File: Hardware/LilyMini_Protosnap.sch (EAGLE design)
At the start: 67 parts, among them Q1 ZXMP6A13F, U1 SAMD11D14A-M, U2 AP2112K-3.3V, U3 ALS-PT19, Y1 32.768kHz

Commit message: Minor tweaks per board review checklist
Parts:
- added LOGO4: SFE_LOGO_NAME.1_INCH, SparkFun-Aesthetics:SFE_LOGO_NAME.1_INCH
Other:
- note added: "NOTE: DO NOT BACKPOWER BOARD THROUGH SEWTAP+ (OUTPUT ONLY) USE AUX VIN (3.5 TO 6V, AVOID CONTENTION WITH USB)"
- note removed: "NOTE: DO NOT BACKPOWER BOARD THROUGH SEWTAP+ (OUTPUT ONLY) USE AUX VIN (3.5 TO 6V)"
- moved on the sheet: D3, D4, D5, D6, R10, R6, R7, R8, R9, S2, U3

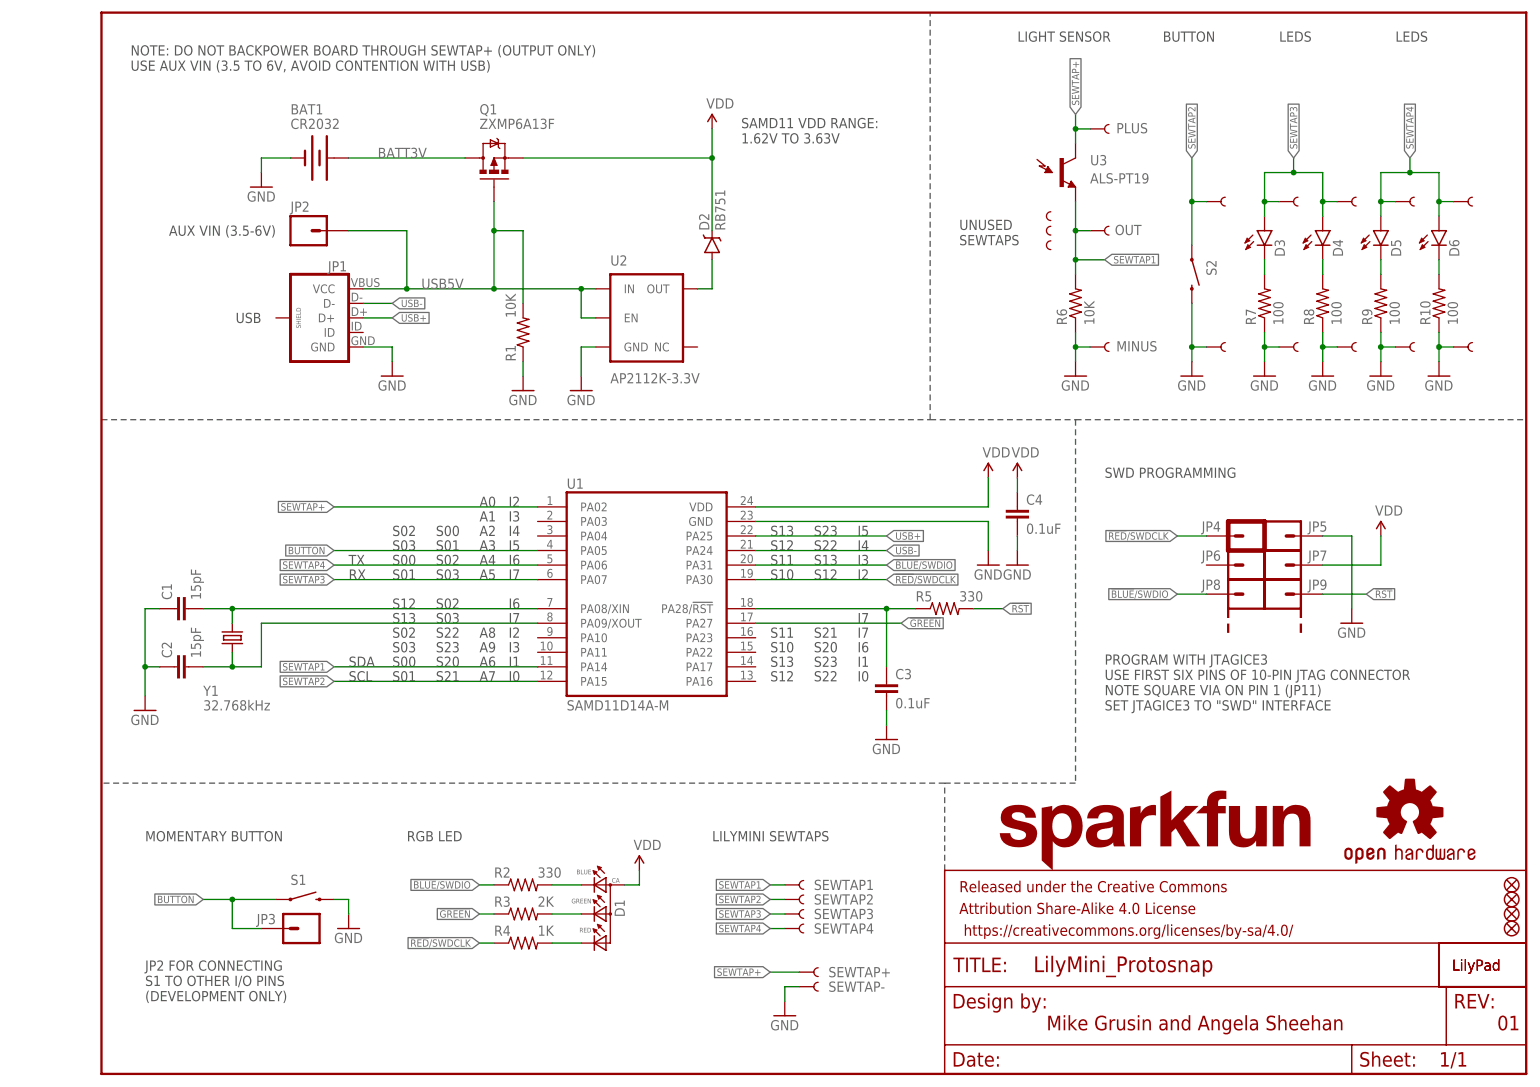
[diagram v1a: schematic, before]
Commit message: Minor changes based on AC and Bob's advice
Reduced paste on QFN and USB footprints by 25%
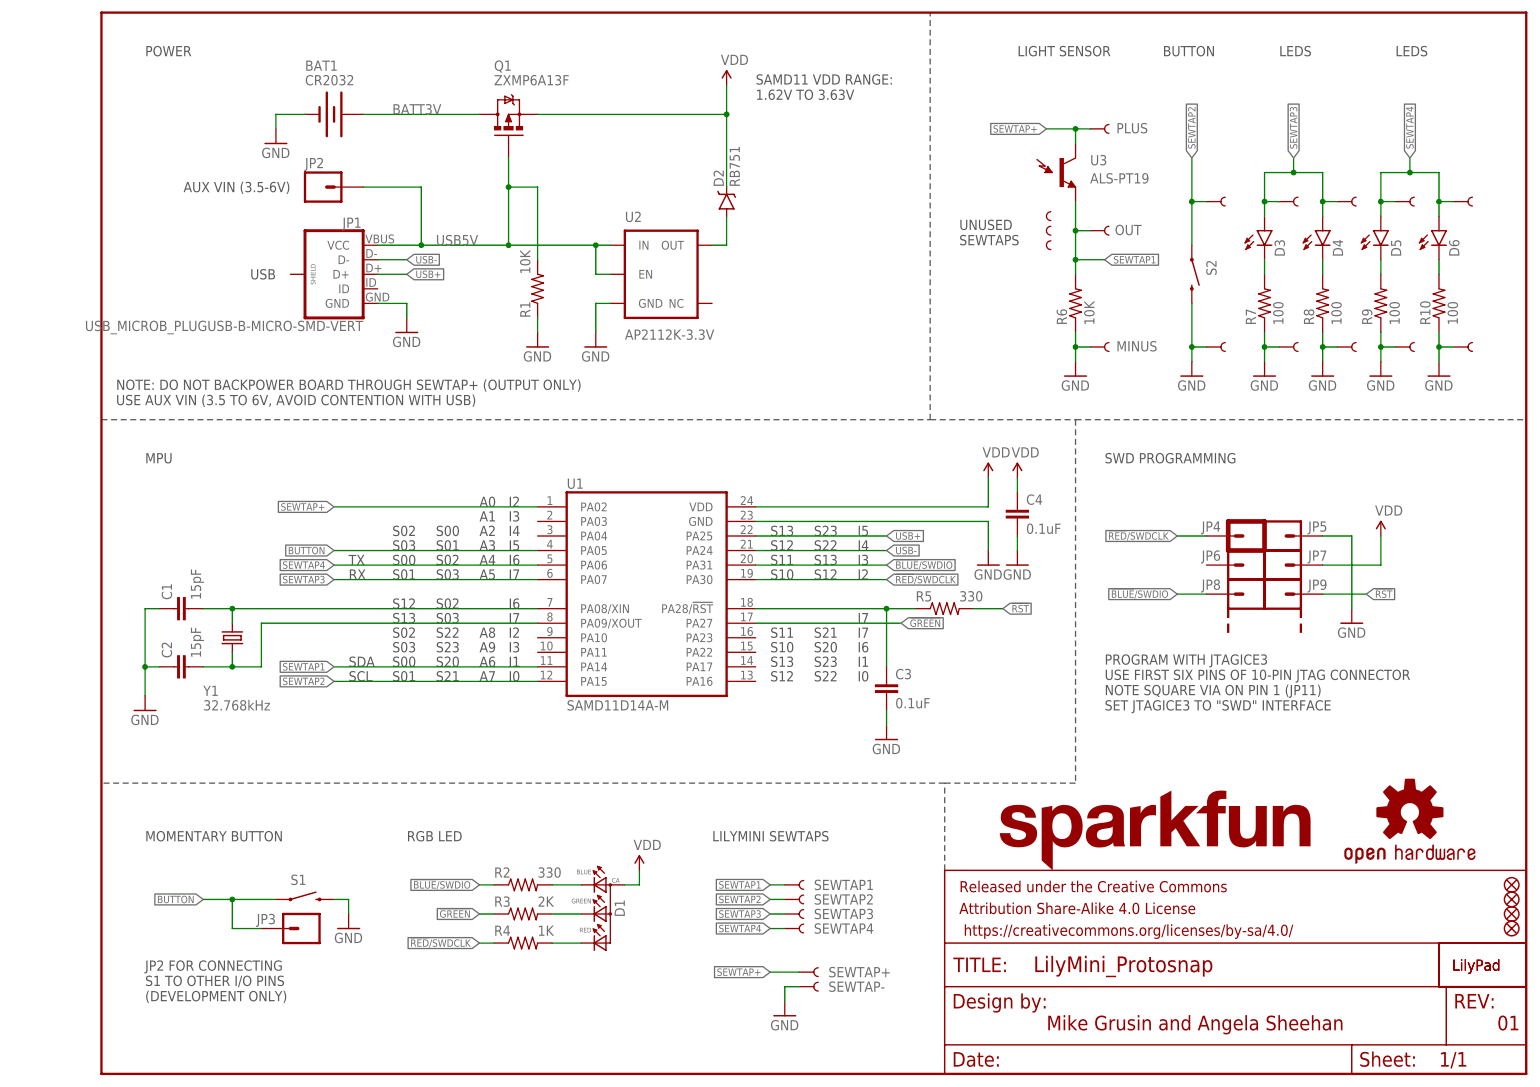
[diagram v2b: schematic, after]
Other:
- note added: "MPU"
- note added: "POWER"
- moved on the sheet: BAT1, D2, JP1, JP2, Q1, R1, U2
